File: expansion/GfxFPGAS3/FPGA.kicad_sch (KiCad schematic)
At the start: 30 parts, among them J1 JTAG, U301 XC3S500E-4PQG208I, U302 W25Q64JVSSIM, Y1 ECS-3963

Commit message: Fix for CXA PAL issue and more
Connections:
- net +1V2: now also U301.117 (VCCINT), U301.13 (VCCINT), U301.170 (VCCINT), U301.67 (VCCINT)
- net +3V3: now also U301.111 (VCCAUX), U301.114 (VCCO_1), U301.125 (VCCO_1), U301.143 (VCCO_1), U301.149 (VCCAUX), U301.166 (VCCAUX), U301.176 (VCCO_0), U301.191 (VCCO_0), U301.195 (VCCAUX), U301.201 (VCCO_0), U301.21 (VCCO_3), U301.38 (VCCO_3), U301.44 (VCCAUX), U301.46 (VCCO_3), U301.59 (VCCO_2), U301.66 (VCCAUX), U301.7 (VCCAUX), U301.73 (VCCO_2), U301.88 (VCCO_2), U301.92 (VCCAUX)
- net A1: now also U301.84 (IO/M1); no longer U301.190 (IO_L11N_0)
- net A10: now also U301.74 (IO_L08P_2/D7/GCLK12); no longer U301.179 (IO/VREF_0)
- net A11: now also U301.69 (IO_L06N_2); no longer U301.178 (IO_L07N_0/GCLK5)
- net A12: now also U301.72 (IP_L07N_2/VREF)
- net A13: now also U301.71 (IP_L07P_2)
- net A14: now also U301.68 (IO_L06P_2); no longer U301.177 (IO_L07P_0/GCLK4)
- net A15: now also U301.65 (IO_L05N_2); no longer U301.172 (IO_L05N_0)
- net A16: now also U301.64 (IO_L05P_2); no longer U301.171 (IO_L05P_0)
- net A17: now also U301.62 (IO_L04P_2); no longer U301.167 (IO_L04P_0)
- net A18: now also U301.63 (IO_L04N_2); no longer U301.168 (IO_L04N_0/VREF_0)
- net A19: now also U301.58 (IO_L01N_2); no longer U301.163 (IO_L02N_0/VREF)
- net A2: now also U301.83 (IO_L11N_2/D1/GCLK3); no longer U301.189 (IO_L11P_0)
- net A3: now also U301.82 (IO_L11P_2/D2/GCLK2); no longer U301.187 (IO)
- net A4: now also U301.81 (IP_L10N_2/M2/GCLK1)
- net A5: now also U301.80 (IP_L10P_2/RDWR_B/GCLK0)
- net A6: now also U301.78 (IO_L09N_2/D3/GCLK15); no longer U301.186 (IO_L10N_0/GCLK11)
- net A7: now also U301.77 (IO_L09P_2/D4/GCLK14); no longer U301.185 (IO_L10P_0/GCLK10)
- net A8: now also U301.76 (IO/D5); no longer U301.181 (IO_L08N_0/GCLK7)
- net A9: now also U301.75 (IO_L08N_2/DD/GCLK13); no longer U301.180 (IO_L08P_0/GCLK6)
- net B0: now also U301.128 (IO_L08P_1/A8/RHCLK2); no longer U301.181 (IO_L08N_0/GCLK7)
- net B1: now also U301.127 (IO_L07N_1/A9/RHCLK1); no longer U301.180 (IO_L08P_0/GCLK6)
- net B2: now also U301.126 (IO_L07P_1/A10/RHCLK0); no longer U301.179 (IO/VREF_0)
- net B3: now also U301.123 (IO_L06N_1/VREF_1); no longer U301.178 (IO_L07N_0/GCLK5)
- net B4: now also U301.122 (IO_L06P_1); no longer U301.177 (IO_L07P_0/GCLK4)
- net B5: now also U301.120 (IO_L05N_1/A11); no longer U301.172 (IO_L05N_0)
- net B6: now also U301.119 (IO_L05P_1/A12); no longer U301.171 (IO_L05P_0)
- net B7: now also U301.116 (IO_L04N_1); no longer U301.168 (IO_L04N_0/VREF_0)
- net CLK_25MHZ: now also U301.103 (IO_L17N_2/CCLK); no longer U301.175 (IP_L06N_0)
- net D0: now also U301.109 (IO_L02N_1/A13); no longer U301.163 (IO_L02N_0/VREF)
- net D1: now also U301.108 (IO_L02P_1/A14); no longer U301.162 (IO_L02P_0)
- net D10: now also U301.94 (IO_L14N_2/A22); no longer U301.200 (IO_L14N_0/VREF_0)
- net D11: now also U301.93 (IO_L14P_2/A23); no longer U301.199 (IO_L14P_0)
- net D12: now also U301.90 (IO_L13N_2); no longer U301.197 (IO_L13N_0)
- net D13: now also U301.89 (IO_L13P_2); no longer U301.196 (IO_L13P_0)
- net D14: now also U301.87 (IO_12N_2/DIN/D0); no longer U301.193 (IO_L12N_0/VREF_0)
- net D15: now also U301.86 (IO_12P_2/M0); no longer U301.192 (IO_L12P_0)
- net D2: now also U301.107 (IO_L01N_1/A15); no longer U301.161 (IO_L01N_0)
- net D3: now also U301.106 (IO_L01P_1/A16); no longer U301.160 (IO_L01P_0)
- net D4: now also U301.102 (IO_L17P_2/VS0/A17); no longer U301.174 (IP_L06P_0)
- net D5: now also U301.100 (IO_L16N_2/VS1/A18)
- net D6: now also U301.99 (IO_L16P_2/VS2/A19); no longer U301.206 (IO_L16N_0/HSWAP)
- net D7: now also U301.98 (IO/VREF_2); no longer U301.205 (IO_L16P_0)
- net D8: now also U301.97 (IO_L15N_2/A20); no longer U301.203 (IO_L15N_0)
- net D9: now also U301.96 (IO_L15P_2/A21); no longer U301.202 (IO_L15P_0)
- net FPGA_DONE: now also U301.104 (DONE)
- net FPGA_INITB: now also U301.56 (IO_L01N_2/INIT_B); no longer U301.161 (IO_L01N_0)
- net FPGA_PROGB: now also U301.1 (PROG_B)
- net G0: now also U301.140 (IO_L12N_1/A0); no longer U301.197 (IO_L13N_0)
- net G1: now also U301.139 (IO_L12P_1); no longer U301.196 (IO_L13P_0)
- net G2: now also U301.138 (IO_L11N_1/A1); no longer U301.193 (IO_L12N_0/VREF_0)
- net G3: now also U301.137 (IO_L11P_1/A2); no longer U301.192 (IO_L12P_0)
- net G4: now also U301.135 (IO_L10N_1/A3/RHCLK7); no longer U301.190 (IO_L11N_0)
- net G5: now also U301.134 (IO_L10P_1/A4/RHCLK6); no longer U301.189 (IO_L11P_0)
- net G6: now also U301.133 (IO_L09N_1/A5/RHCLK5); no longer U301.187 (IO)
- net G7: now also U301.132 (IO_L09P_1/A6/RHCLK4/IRDY1); no longer U301.186 (IO_L10N_0/GCLK11)
- net GND: now also U301.10 (GND), U301.105 (GND), U301.121 (GND), U301.131 (GND), U301.141 (GND), U301.156 (GND), U301.17 (GND), U301.173 (GND), U301.182 (GND), U301.188 (GND), U301.198 (GND), U301.208 (GND), U301.27 (GND), U301.37 (GND), U301.52 (GND), U301.53 (GND), U301.70 (GND), U301.79 (GND), U301.85 (GND), U301.95 (GND)
- net HSYNC: now also U301.112 (IO_L03P_1); no longer U301.164 (IO_L03P_0)
- net PIXELCLOCK: now also U301.115 (IO_L04P_1); no longer U301.167 (IO_L04P_0)
- net R0: now also U301.153 (IO_L16N_1/LDC2); no longer U301.174 (IP_L06P_0)
- net R1: now also U301.152 (IO_L16P_1/LDC1)
- net R2: now also U301.151 (IO_L15N_1/LDC0); no longer U301.206 (IO_L16N_0/HSWAP)
- net R3: now also U301.150 (IO_L15P_1/HDC); no longer U301.205 (IO_L16P_0)
- net R4: now also U301.147 (IO_L14N_1); no longer U301.203 (IO_L15N_0)
- net R5: now also U301.146 (IO_L14P_1); no longer U301.202 (IO_L15P_0)
- net R6: now also U301.145 (IO_L13N_1); no longer U301.200 (IO_L14N_0/VREF_0)
- net R7: now also U301.144 (IO_L13P_1); no longer U301.199 (IO_L14P_0)
- net SRAM_A5: now also U301.29 (IO_L09N_3/LHCLK5); no longer U301.187 (IO)
- net SRAM_A6: now also U301.28 (IO_L09P_3/LHCLK3/TRDY2); no longer U301.186 (IO_L10N_0/GCLK11)
- net SRAM_A7: now also U301.25 (IO_L08N_3/LHCLK3/IRDY2); no longer U301.185 (IO_L10P_0/GCLK10)
- net SRAM_A8: now also U301.24 (IO_L08P_3/LHCLK2); no longer U301.181 (IO_L08N_0/GCLK7)
- net SRAM_D0: now also U301.2 (IO_L01P_3); no longer U301.160 (IO_L01P_0)
- net SRAM_D1: now also U301.3 (IO_L01N_3); no longer U301.161 (IO_L01N_0)
- net SRAM_D10: now also U301.40 (IO_L13N_3); no longer U301.200 (IO_L14N_0/VREF_0)
- net SRAM_D11: now also U301.39 (IO_L13P_3); no longer U301.199 (IO_L14P_0)
- net SRAM_D12: now also U301.36 (IO_L12N_3); no longer U301.197 (IO_L13N_0)
- net SRAM_D13: now also U301.35 (IO_L12P_3); no longer U301.196 (IO_L13P_0)
- net SRAM_D14: now also U301.34 (IO_L11N_3); no longer U301.193 (IO_L12N_0/VREF_0)
- net SRAM_D15: now also U301.33 (IO_L11P_3); no longer U301.192 (IO_L12P_0)
- net SRAM_D2: now also U301.4 (IO_L02P_3); no longer U301.162 (IO_L02P_0)
- net SRAM_D28: now also U301.15 (IO_L05P_3); no longer U301.171 (IO_L05P_0)
- net SRAM_D29: now also U301.16 (IO_L05N_3); no longer U301.172 (IO_L05N_0)
- net SRAM_D3: now also U301.5 (IO_L02N_3/VREF); no longer U301.163 (IO_L02N_0/VREF)
- net SRAM_D30: now also U301.18 (IO_L06P_3); no longer U301.177 (IO_L07P_0/GCLK4)
- net SRAM_D31: now also U301.19 (IO_L06N_3); no longer U301.178 (IO_L07N_0/GCLK5)
- net SRAM_D4: now also U301.8 (IO_L03P_3); no longer U301.164 (IO_L03P_0)
- net SRAM_D5: now also U301.9 (IO_L03N_P); no longer U301.165 (IO_L03N_0)
- net SRAM_D6: now also U301.11 (IO_L04P_3); no longer U301.167 (IO_L04P_0)
- net SRAM_D7: now also U301.12 (IO_L03N_3); no longer U301.168 (IO_L04N_0/VREF_0)
- net SRAM_D8: now also U301.42 (IO_L14N_3); no longer U301.203 (IO_L15N_0)
- net SRAM_D9: now also U301.41 (IO_L14P_3); no longer U301.202 (IO_L15P_0)
- net VSYNC: now also U301.113 (IO_L03N_1/VREF); no longer U301.165 (IO_L03N_0)
- net ~{BLANK}: now also U301.129 (IO_L08N_1/A7/RHCLK3/TRDY1); no longer U301.185 (IO_L10P_0/GCLK10)
- net ~{SRAM_LB0}: now also U301.31 (IO_L10N_3/LHCLK7); no longer U301.190 (IO_L11N_0)
- net ~{SRAM_LB1}: now also U301.22 (IO_L07P_3/LHCLK0); no longer U301.179 (IO/VREF_0)
- net ~{SRAM_UB0}: now also U301.30 (IO_L10P_3/LHCLK6); no longer U301.189 (IO_L11P_0)
- net ~{SRAM_UB1}: now also U301.23 (IO_L07N_3/LHCLK1); no longer U301.180 (IO_L08P_0/GCLK6)
- net at J1.3 (Pin_3): now also U301.207 (TDI); no longer U301.202 (IO_L15P_0)
- net at J1.2 (Pin_2): now also U301.158 (TCK)
- net at J1.4 (Pin_4): now also U301.157 (TDO)
- net at J1.5 (Pin_5): now also U301.155 (TMS)
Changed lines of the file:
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@@
     (pin "1")
   )
-  (symbol (lib_id "Ddraig:XC3S500E-4PQG208I") (at 77.47 109.22 0)
+  (symbol (lib_id "Ddraig:XC3S500E-4PQG208I") (at 77.47 109.22 0) (unit 1)
     (in_bom yes) (on_board yes)
     (property "Reference" "U301" (id 0) (at 62.23 167.64 0)
@@
     (pin "206")
   )
-  (symbol (lib_id "Ddraig:XC3S500E-4PQG208I") (at 167.64 109.22 0)
+  (symbol (lib_id "Ddraig:XC3S500E-4PQG208I") (at 167.64 109.22 0) (unit 2)
     (in_bom yes) (on_board yes)
     (property "Reference" "U301" (id 0) (at 152.4 167.64 0)
@@
     (pin "154")
   )
-  (symbol (lib_id "Ddraig:XC3S500E-4PQG208I") (at 265.43 109.22 0)
+  (symbol (lib_id "Ddraig:XC3S500E-4PQG208I") (at 265.43 109.22 0) (unit 3)
     (in_bom yes) (on_board yes)
     (property "Reference" "U301" (id 0) (at 250.19 167.64 0)
@@
     (pin "1")
   )
-  (symbol (lib_id "Ddraig:XC3S500E-4PQG208I") (at 364.49 109.22 0)
+  (symbol (lib_id "Ddraig:XC3S500E-4PQG208I") (at 364.49 109.22 0) (unit 4)
     (in_bom yes) (on_board yes)
     (property "Reference" "U301" (id 0) (at 349.25 167.64 0)
@@
     (pin "1")
   )
-  (symbol (lib_id "Ddraig:XC3S500E-4PQG208I") (at 73.66 241.3 0)
+  (symbol (lib_id "Ddraig:XC3S500E-4PQG208I") (at 73.66 241.3 0) (unit 5)
     (in_bom yes) (on_board yes)
     (property "Reference" "U301" (id 0) (at 60.96 190.5 0))
@@
     (pin "2")
   )
-  (symbol (lib_id "Ddraig:XC3S500E-4PQG208I") (at 384.81 236.22 0)
+  (symbol (lib_id "Ddraig:XC3S500E-4PQG208I") (at 384.81 236.22 0) (unit 6)
     (in_bom yes) (on_board yes)
     (property "Reference" "U301" (id 0) (at 382.27 222.25 0)
@@
     (pin "2")
   )
-  (symbol (lib_id "Device:C") (at 242.57 30.48 0)
+  (symbol (lib_id "Device:C") (at 242.57 30.48 0) (unit 1)
     (in_bom yes) (on_board yes)
     (property "Reference" "C304" (id 0) (at 245.491 29.3116 0)
@@
     (pin "2")
   )
-  (symbol (lib_id "power:GND") (at 236.22 39.37 0)
+  (symbol (lib_id "power:GND") (at 236.22 39.37 0) (unit 1)
     (in_bom yes) (on_board yes)
     (property "Reference" "#PWR0305" (id 0) (at 236.22 45.72 0)
@@
     (pin "1")
   )
-  (symbol (lib_id "Device:C") (at 255.27 30.48 0)
+  (symbol (lib_id "Device:C") (at 255.27 30.48 0) (unit 1)
     (in_bom yes) (on_board yes)
     (property "Reference" "C305" (id 0) (at 258.191 29.3116 0)
@@
     (pin "2")
   )
-  (symbol (lib_id "Device:C") (at 269.24 30.48 0)
+  (symbol (lib_id "Device:C") (at 269.24 30.48 0) (unit 1)
     (in_bom yes) (on_board yes)
     (property "Reference" "C306" (id 0) (at 272.161 29.3116 0)
@@
     (pin "2")
   )
-  (symbol (lib_id "Device:C") (at 203.2 30.48 0)
+  (symbol (lib_id "Device:C") (at 203.2 30.48 0) (unit 1)
     (in_bom yes) (on_board yes)
     (property "Reference" "C301" (id 0) (at 206.121 29.3116 0)
@@
     (pin "2")
   )
-  (symbol (lib_id "Device:C") (at 215.9 30.48 0)
+  (symbol (lib_id "Device:C") (at 215.9 30.48 0) (unit 1)
     (in_bom yes) (on_board yes)
     (property "Reference" "C302" (id 0) (at 218.821 29.3116 0)
@@
     (pin "2")
   )
-  (symbol (lib_id "Device:C") (at 229.87 30.48 0)
+  (symbol (lib_id "Device:C") (at 229.87 30.48 0) (unit 1)
     (in_bom yes) (on_board yes)
     (property "Reference" "C303" (id 0) (at 232.791 29.3116 0)
@@
     (pin "2")
   )
-  (symbol (lib_id "power:+3V3") (at 236.22 21.59 0)
+  (symbol (lib_id "power:+3V3") (at 236.22 21.59 0) (unit 1)
     (in_bom yes) (on_board yes)
     (property "Reference" "#PWR0304" (id 0) (at 236.22 25.4 0)
@@
     (pin "1")
   )
-  (symbol (lib_id "Device:C") (at 160.02 30.48 0)
+  (symbol (lib_id "Device:C") (at 160.02 30.48 0) (unit 1)
     (in_bom yes) (on_board yes)
     (property "Reference" "C308" (id 0) (at 162.941 29.3116 0)
@@
     (pin "2")
   )
-  (symbol (lib_id "power:GND") (at 166.37 39.37 0)
+  (symbol (lib_id "power:GND") (at 166.37 39.37 0) (unit 1)
     (in_bom yes) (on_board yes)
     (property "Reference" "#PWR0117" (id 0) (at 166.37 45.72 0)
@@
     (pin "1")
   )
-  (symbol (lib_id "Device:C") (at 172.72 30.48 0)
+  (symbol (lib_id "Device:C") (at 172.72 30.48 0) (unit 1)
     (in_bom yes) (on_board yes)
     (property "Reference" "C309" (id 0) (at 175.641 29.3116 0)
@@
     (pin "2")
   )
-  (symbol (lib_id "Device:C") (at 186.69 30.48 0)
+  (symbol (lib_id "Device:C") (at 186.69 30.48 0) (unit 1)
     (in_bom yes) (on_board yes)
     (property "Reference" "C310" (id 0) (at 189.611 29.3116 0)
@@
     (pin "2")
   )
-  (symbol (lib_id "Device:C") (at 147.32 30.48 0)
+  (symbol (lib_id "Device:C") (at 147.32 30.48 0) (unit 1)
     (in_bom yes) (on_board yes)
     (property "Reference" "C307" (id 0) (at 150.241 29.3116 0)

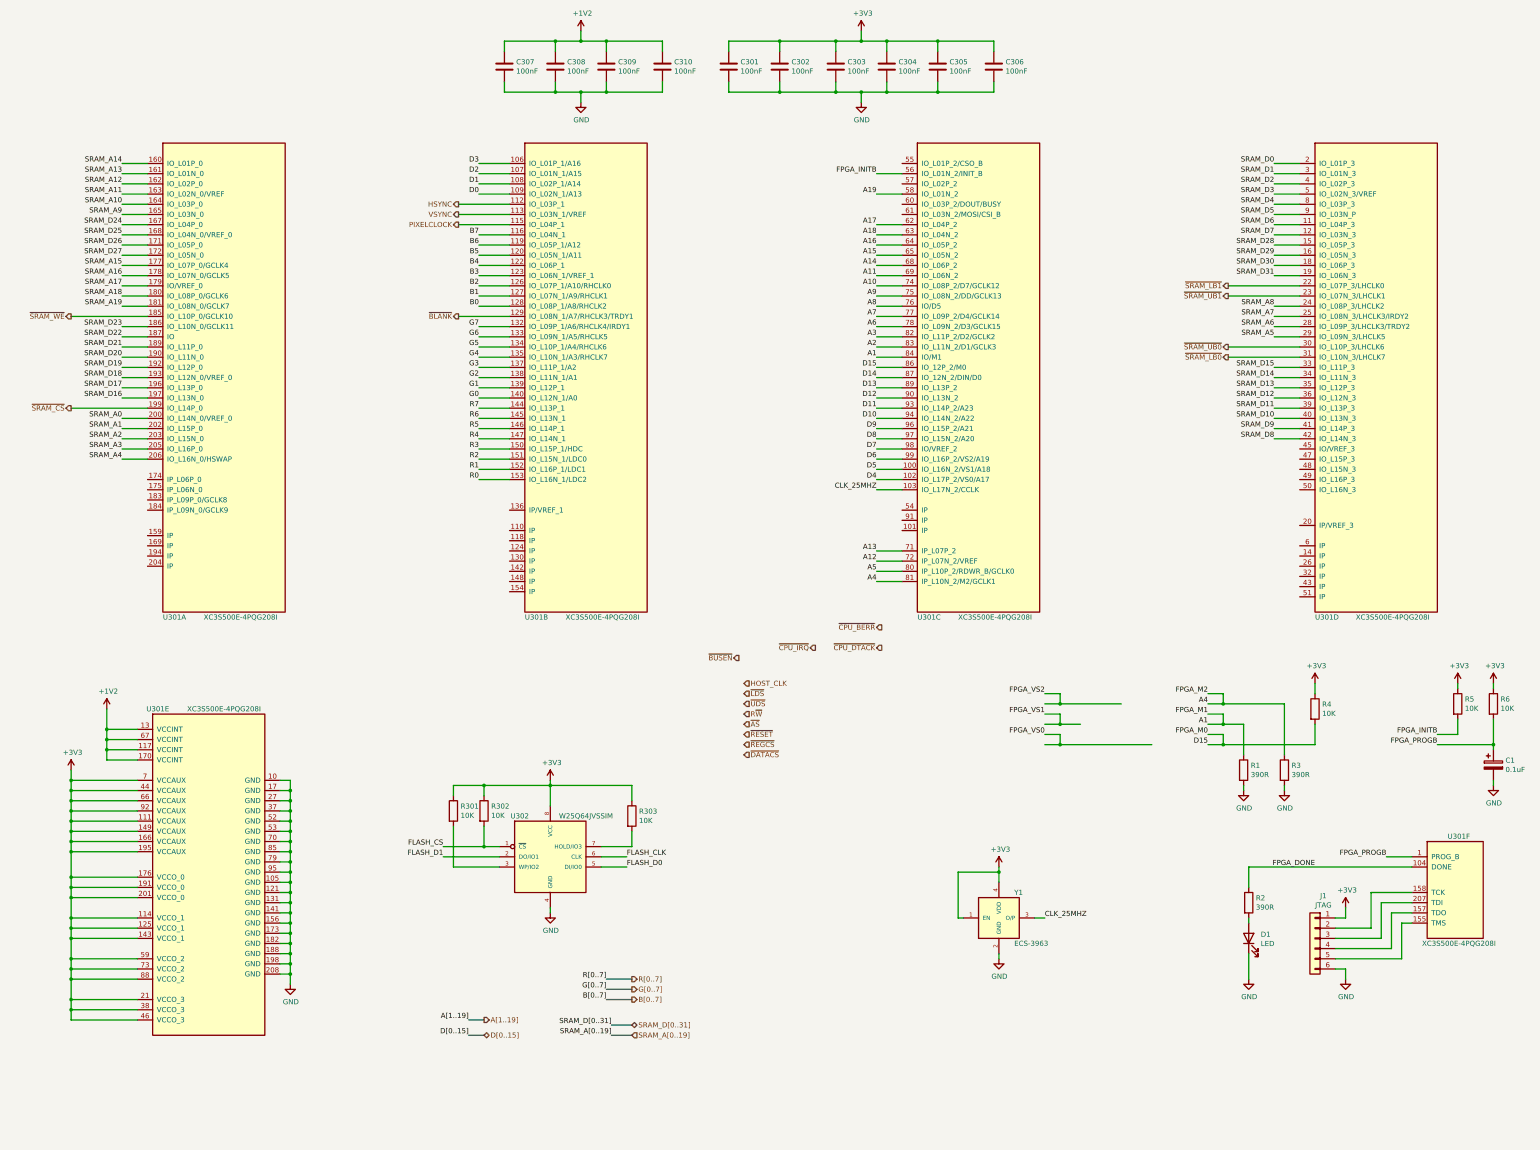
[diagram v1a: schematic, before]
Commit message: More progress on Spartan-3 FPGA board
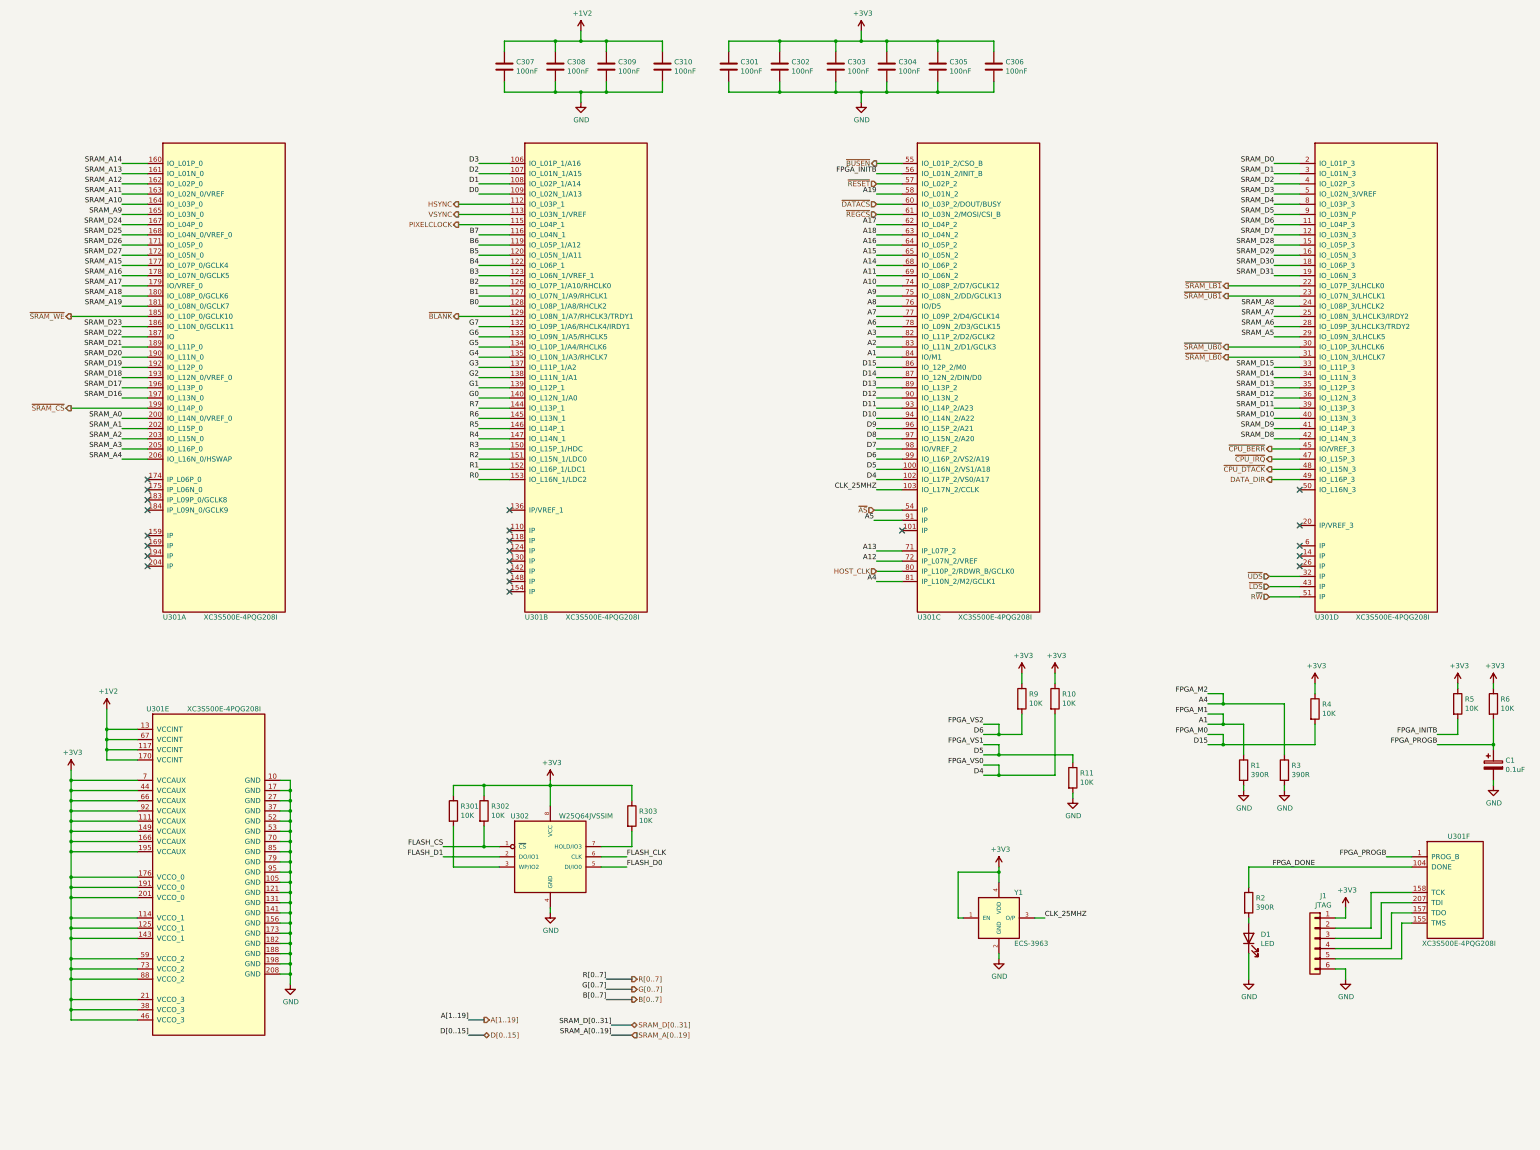
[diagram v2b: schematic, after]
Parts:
- added R10, R11, R9: 10K, symbol Device:R
- C1: symbol Device:CP -> Device:C_Polarized
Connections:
- net +3V3: now also R10.1, R9.1
- net A5: now also U301.91 (IP); no longer U301.80 (IP_L10P_2/RDWR_B/GCLK0)
- net D4: now also R10.2
- net D5: now also R11.1
- net D6: now also R9.2
- net GND: now also R11.2
- net HOST_CLK: now also U301.80 (IP_L10P_2/RDWR_B/GCLK0)
- net R~{W}: now also U301.51 (IP)
- net ~{AS}: now also U301.54 (IP)
- net ~{BUSEN}: now also U301.55 (IO_L01P_2/CSO_B)
- net ~{CPU_BERR}: now also U301.45 (IO/VREF_3)
- net ~{CPU_DTACK}: now also U301.48 (IO_L15N_3)
- net ~{CPU_IRQ}: now also U301.47 (IO_L15P_3)
- net ~{DATACS}: now also U301.60 (IO_L03P_2/DOUT/BUSY)
- net ~{LDS}: now also U301.43 (IP)
- net ~{REGCS}: now also U301.61 (IO_L03N_2/MOSI/CSI_B)
- net ~{RESET}: now also U301.57 (IO_L02P_2)
- net ~{UDS}: now also U301.32 (IP)
- net DATA_DIR: now reaches U301.49 (IO_L16P_3)
- no-connect marks 0 -> 22

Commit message: Part placement on video card
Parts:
- added D2: LED, LED_SMD:LED_1206_3216Metric, symbol Device:LED
- added R12: 390R, Resistor_SMD:R_0805_2012Metric, symbol Device:R
- C1: footprint (none) -> Capacitor_SMD:CP_Elec_4x5.3
- J1: footprint (none) -> Connector_PinHeader_2.54mm:PinHeader_1x06_P2.54mm_Vertical
- R1, R10, R11, R2, R3, R4, R5, R6, R9: footprint (none) -> Resistor_SMD:R_0805_2012Metric
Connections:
- net +3V3: now also R12.1
- net SRAM_A5: now also U301.24 (IO_L08P_3/LHCLK2); no longer U301.29 (IO_L09N_3/LHCLK5)
- net SRAM_A6: now also U301.25 (IO_L08N_3/LHCLK3/IRDY2); no longer U301.28 (IO_L09P_3/LHCLK3/TRDY2)
- net SRAM_A7: now also U301.28 (IO_L09P_3/LHCLK3/TRDY2); no longer U301.25 (IO_L08N_3/LHCLK3/IRDY2)
- net SRAM_A8: now also U301.29 (IO_L09N_3/LHCLK5); no longer U301.24 (IO_L08P_3/LHCLK2)
- net ~{ACCESS_LED}: now reaches U301.50 (IO_L16N_3)
- net ~{ACCESS_LED}: now also D2.1 (K)
- new net: D2.2 (A), R12.2
- no-connect marks 22 -> 21
